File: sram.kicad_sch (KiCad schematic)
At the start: 5 parts, among them J1 SRAM_pinheader_DIP32, U1 628128_TSOP32

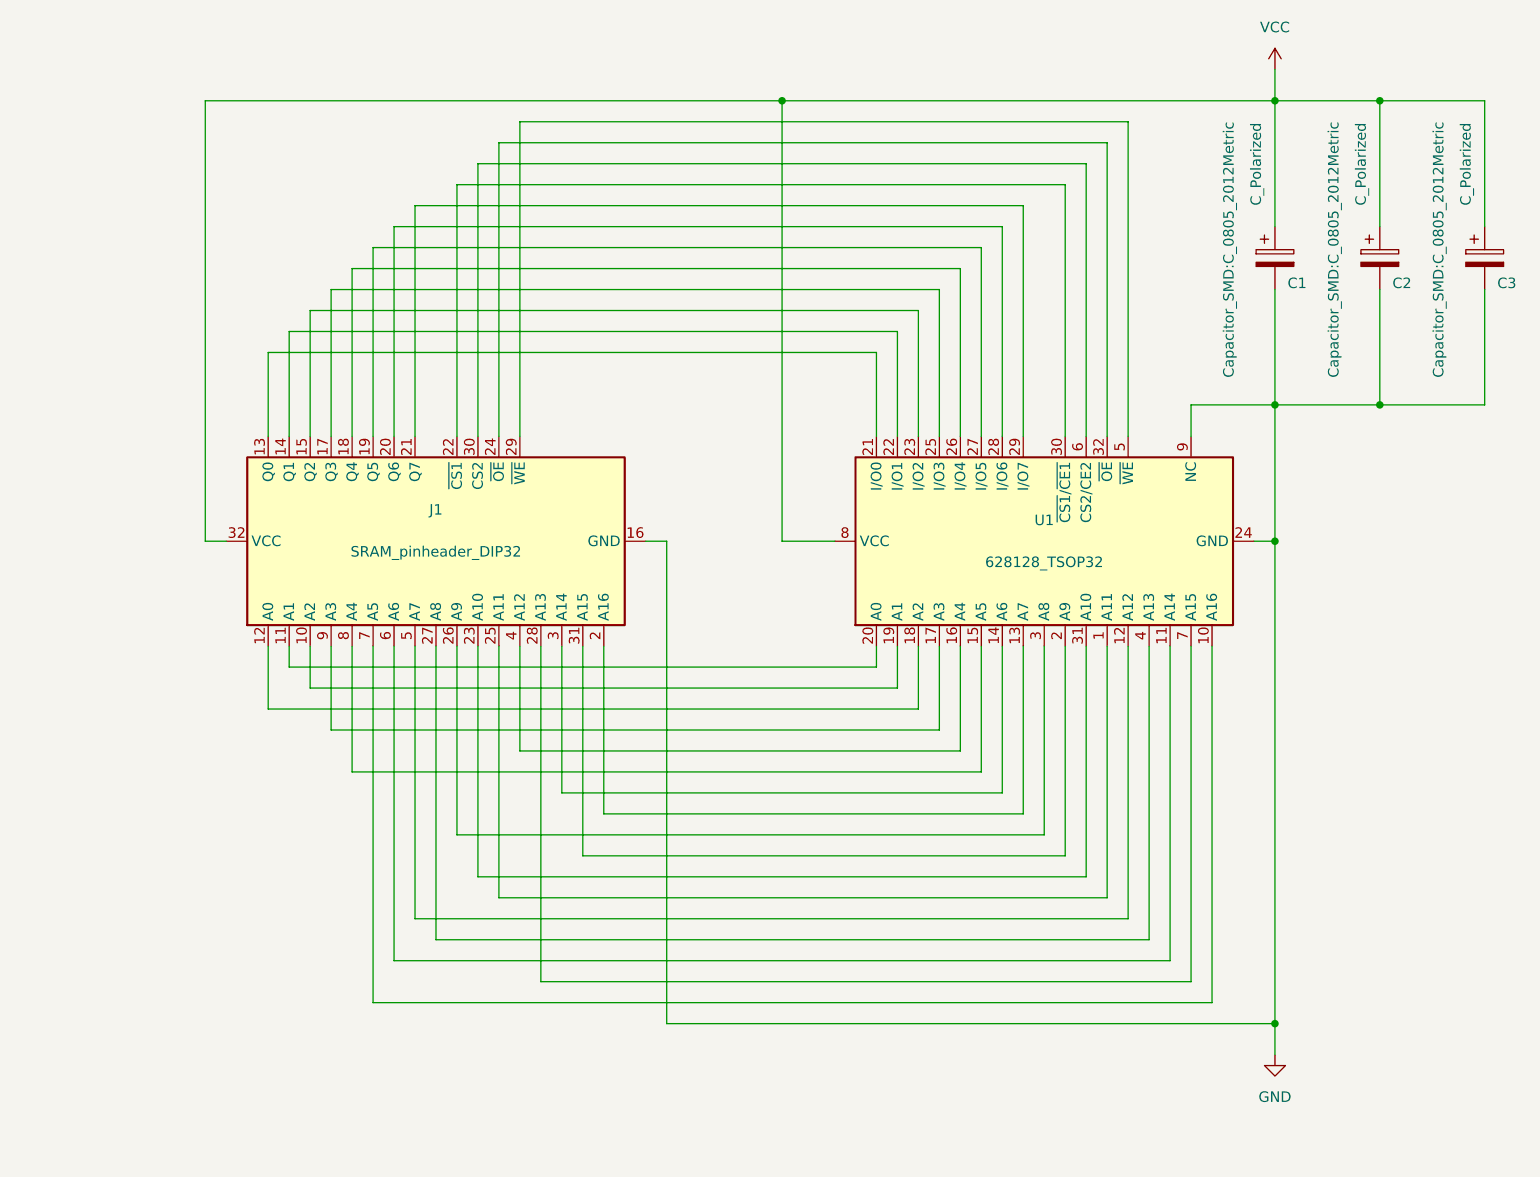
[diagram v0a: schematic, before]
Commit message: Better labels for decoupling caps
Added DIP pinheader 3D model

Signed-off-by: Petr Cvek <petrcvekcz@gmail.com>
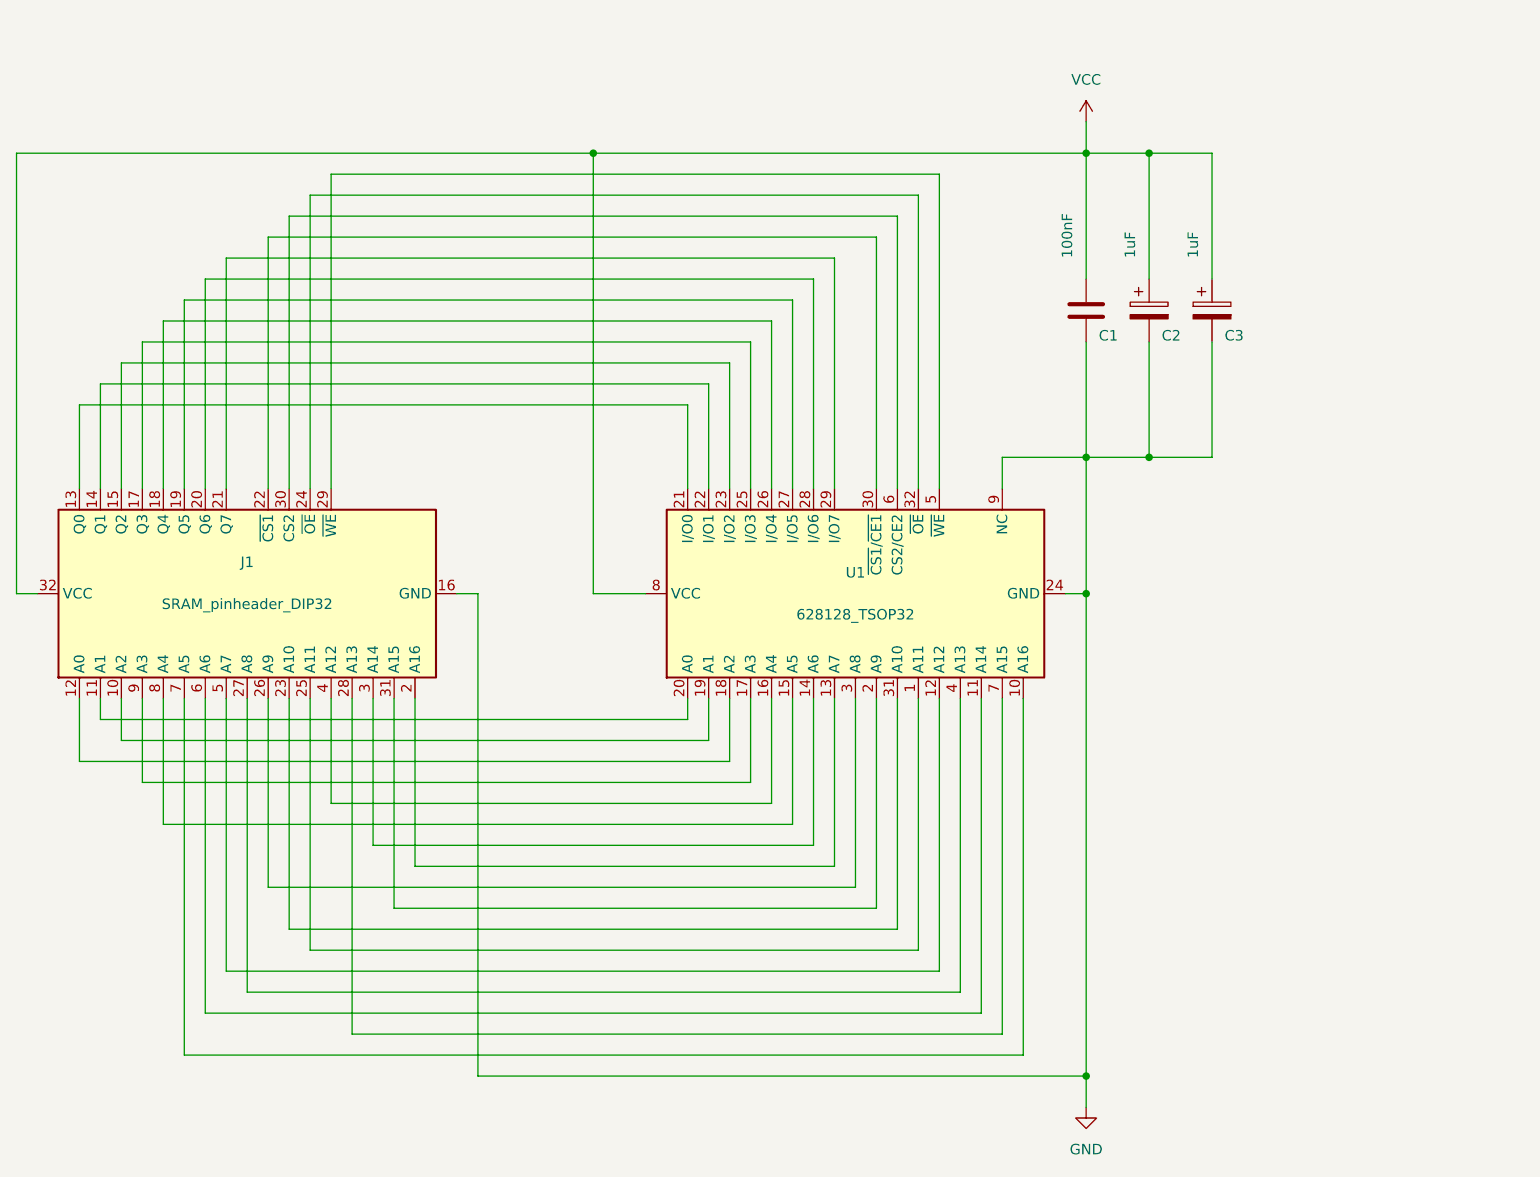
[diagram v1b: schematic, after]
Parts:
- C1: value C_Polarized -> 100nF; symbol Device:C_Polarized -> Device:C
- C2, C3: value C_Polarized -> 1uF
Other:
- moved on the sheet: C2, C3, J1, U1
